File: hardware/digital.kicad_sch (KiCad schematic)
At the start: 24 parts, among them J3 Pin Header Male, Q6 DTC114E, Q7 DTC114E, Q8 DTC114E, Q9 DTC114E, U6 ATmega88PA-AU, U7 QDSP-6064

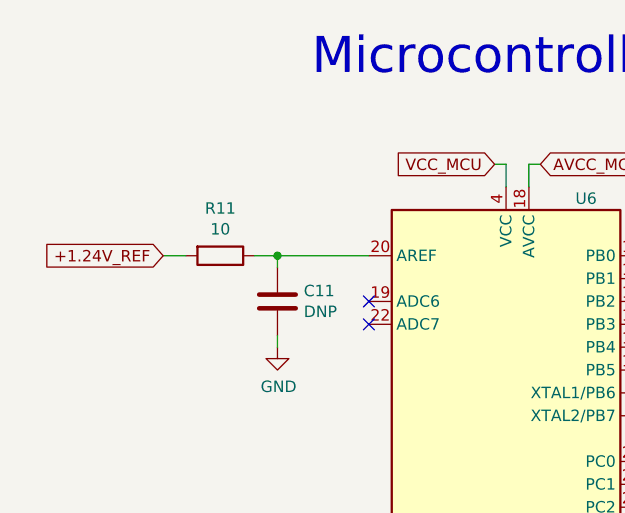
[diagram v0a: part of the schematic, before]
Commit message: Change R11 to 100 ohm
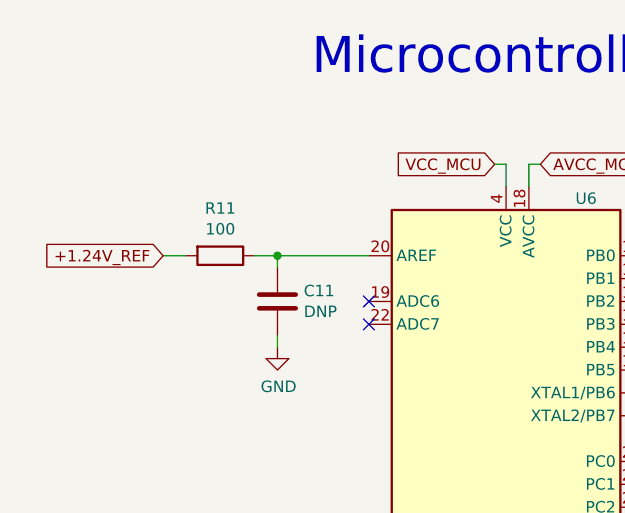
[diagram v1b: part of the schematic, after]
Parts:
- R11: value 10 -> 100
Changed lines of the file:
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@@
       (effects (font (size 1.27 1.27)))
     )
-    (property "Value" "10" (at 44.45 45.3136 90)
+    (property "Value" "100" (at 44.45 45.3136 90)
       (effects (font (size 1.27 1.27)))
     )
